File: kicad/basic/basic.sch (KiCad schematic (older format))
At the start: 20 parts, among them P2 CONN_01X15, P3 CONN_01X15, P4 CONN_01X06, P5 CONN_01X01, P6 CONN_01X01, P7 CONN_01X01, P8 CONN_01X01, P9 CONN_01X06, SW1 SW_PUSH, SW2 SW_PUSH

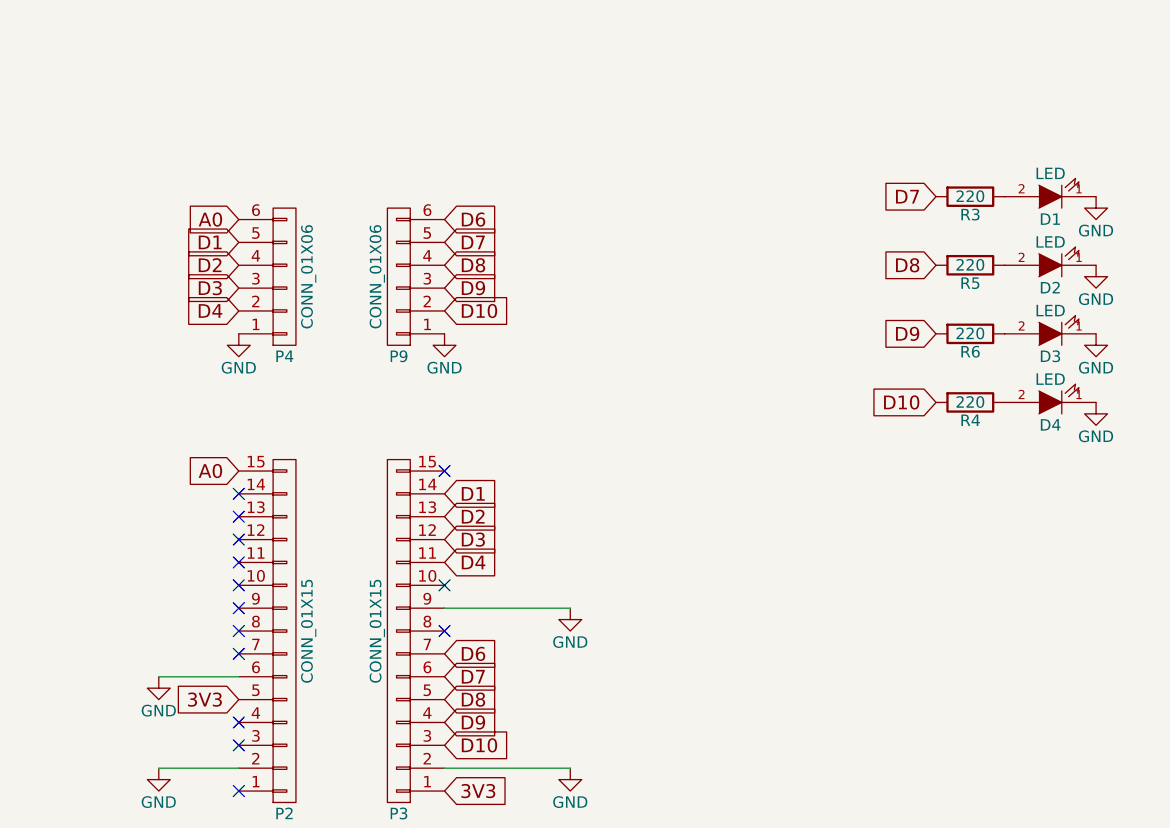
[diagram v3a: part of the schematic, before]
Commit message: RGB led
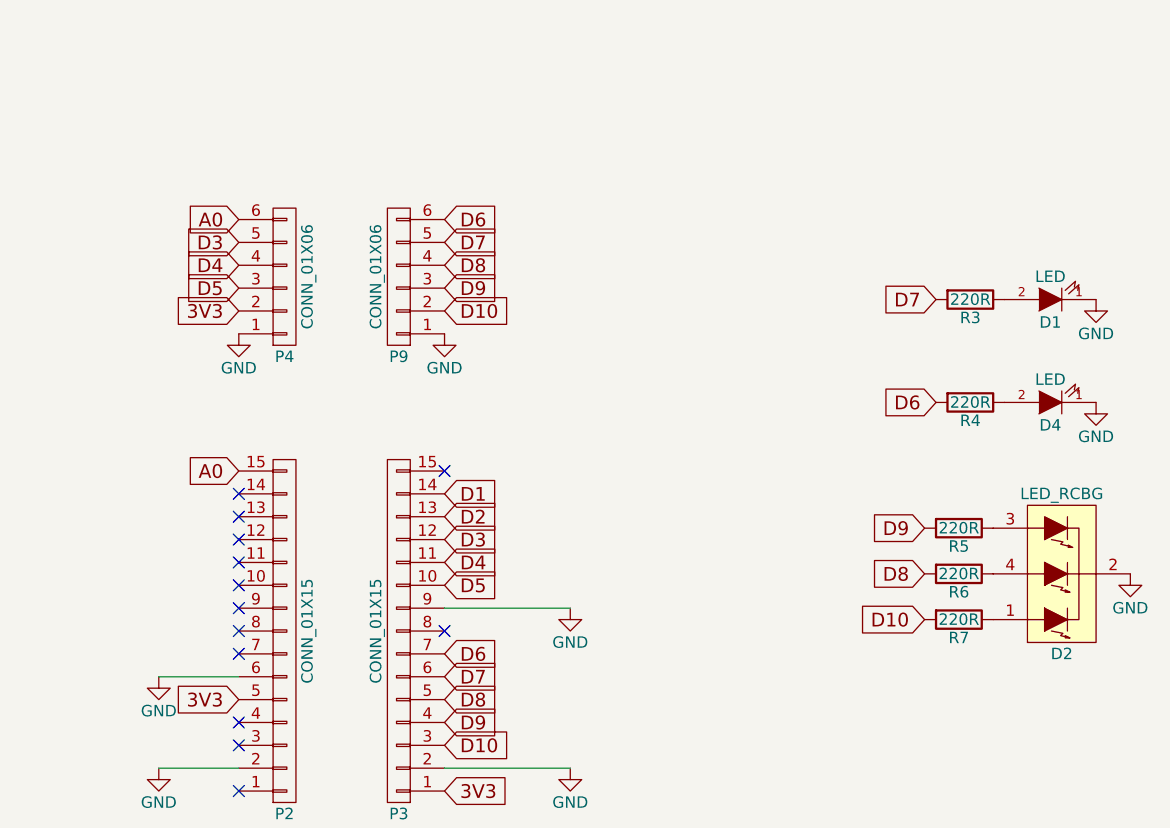
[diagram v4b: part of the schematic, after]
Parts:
- removed D2, D3: LED, LEDs:LED-5MM, symbol LED
- added D2: LED_RCBG, LEDs:LED-RGB-5MM_Common_Cathode, symbol LED_RCBG
- added R7: 220R, Resistors_ThroughHole:Resistor_Horizontal_RM10mm, symbol R
- R3, R4, R5, R6: value 220 -> 220R
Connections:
- net 3V3: now also P4.2 (P2)
- net D1: no longer P4.5 (P5)
- net D10: now also R7.2; no longer R4.2
- net D2: no longer P4.4 (P4)
- net D3: now also P4.5 (P5); no longer P4.3 (P3)
- net D4: now also P4.4 (P4); no longer P4.2 (P2)
- net D6: now also R4.2
- net D8: now also R6.2; no longer R5.2
- net D9: now also R5.2; no longer R6.2
- net GND: now also D2.2 (COMMON_CATHODE)
- net at R6.1: now also D2.4 (GREEN_ANODE)
- net at R5.1: now also D2.3 (BLUE_ANODE)
- net D5: now reaches P3.10 (P10)
- net D5: now also P4.3 (P3)
- new net: D2.1 (RED_ANODE), R7.1
- no-connect marks 14 -> 13
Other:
- moved on the sheet: D1, R3, R5, R6
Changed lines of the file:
@@
 P 8700 3200
 F 0 "R4" V 8780 3200 50  0000 C CNN
-F 1 "220" V 8700 3200 50  0000 C CNN
+F 1 "220R" V 8700 3200 50  0000 C CNN
 F 2 "Resistors_ThroughHole:Resistor_Horizontal_RM10mm" V 8630 3200 50  0001 C CNN
 F 3 "" H 8700 3200 50  0000 C CNN
@@
 $EndComp
 $Comp
-L LED D3
-U 1 1 570F8E13
-P 9050 2900
-F 0 "D3" H 9050 3000 50  0000 C CNN
-F 1 "LED" H 9050 2800 50  0000 C CNN
-F 2 "LEDs:LED-5MM" H 9050 2900 50  0001 C CNN
-F 3 "" H 9050 2900 50  0000 C CNN
-	1    9050 2900
-	-1   0    0    1
-$EndComp
-$Comp
 L R R6
 U 1 1 570F8E19
-P 8700 2900
-F 0 "R6" V 8780 2900 50  0000 C CNN
-F 1 "220" V 8700 2900 50  0000 C CNN
-F 2 "Resistors_ThroughHole:Resistor_Horizontal_RM10mm" V 8630 2900 50  0001 C CNN
-F 3 "" H 8700 2900 50  0000 C CNN
-	1    8700 2900
+P 8650 3950
+F 0 "R6" V 8730 3950 50  0000 C CNN
+F 1 "220R" V 8650 3950 50  0000 C CNN
+F 2 "Resistors_ThroughHole:Resistor_Horizontal_RM10mm" V 8580 3950 50  0001 C CNN
+F 3 "" H 8650 3950 50  0000 C CNN
+	1    8650 3950
 	0    1    1    0
-$EndComp
-$Comp
-L LED D2
-U 1 1 570F8EB1
-P 9050 2600
-F 0 "D2" H 9050 2700 50  0000 C CNN
-F 1 "LED" H 9050 2500 50  0000 C CNN
-F 2 "LEDs:LED-5MM" H 9050 2600 50  0001 C CNN
-F 3 "" H 9050 2600 50  0000 C CNN
-	1    9050 2600
-	-1   0    0    1
 $EndComp
 $Comp
 L R R5
 U 1 1 570F8EB7
-P 8700 2600
-F 0 "R5" V 8780 2600 50  0000 C CNN
-F 1 "220" V 8700 2600 50  0000 C CNN
-F 2 "Resistors_ThroughHole:Resistor_Horizontal_RM10mm" V 8630 2600 50  0001 C CNN
-F 3 "" H 8700 2600 50  0000 C CNN
-	1    8700 2600
+P 8650 3750
+F 0 "R5" V 8730 3750 50  0000 C CNN
+F 1 "220R" V 8650 3750 50  0000 C CNN
+F 2 "Resistors_ThroughHole:Resistor_Horizontal_RM10mm" V 8580 3750 50  0001 C CNN
+F 3 "" H 8650 3750 50  0000 C CNN
+	1    8650 3750
 	0    1    1    0
 $EndComp
@@
 L LED D1
 U 1 1 570F8EBD
-P 9050 2300
-F 0 "D1" H 9050 2400 50  0000 C CNN
-F 1 "LED" H 9050 2200 50  0000 C CNN
-F 2 "LEDs:LED-5MM" H 9050 2300 50  0001 C CNN
-F 3 "" H 9050 2300 50  0000 C CNN
-	1    9050 2300
+P 9050 2750
+F 0 "D1" H 9050 2850 50  0000 C CNN
+F 1 "LED" H 9050 2650 50  0000 C CNN
+F 2 "LEDs:LED-5MM" H 9050 2750 50  0001 C CNN
+F 3 "" H 9050 2750 50  0000 C CNN
+	1    9050 2750
 	-1   0    0    1
 $EndComp
@@
 L R R3
 U 1 1 570F8EC3
-P 8700 2300
-F 0 "R3" V 8780 2300 50  0000 C CNN
-F 1 "220" V 8700 2300 50  0000 C CNN
-F 2 "Resistors_ThroughHole:Resistor_Horizontal_RM10mm" V 8630 2300 50  0001 C CNN
-F 3 "" H 8700 2300 50  0000 C CNN
-	1    8700 2300
+P 8700 2750
+F 0 "R3" V 8780 2750 50  0000 C CNN
+F 1 "220R" V 8700 2750 50  0000 C CNN
+F 2 "Resistors_ThroughHole:Resistor_Horizontal_RM10mm" V 8630 2750 50  0001 C CNN
+F 3 "" H 8700 2750 50  0000 C CNN
+	1    8700 2750
 	0    1    1    0
 $EndComp
 $Comp
 L GND #PWR06
-U 1 1 570F8F9B
-P 9250 2900
-F 0 "#PWR06" H 9250 2650 50  0001 C CNN
-F 1 "GND" H 9250 2750 50  0000 C CNN
-F 2 "" H 9250 2900 50  0000 C CNN
-F 3 "" H 9250 2900 50  0000 C CNN
-	1    9250 2900
+U 1 1 570F8FDF
+P 9400 3950
+F 0 "#PWR06" H 9400 3700 50  0001 C CNN
+F 1 "GND" H 9400 3800 50  0000 C CNN
+F 2 "" H 9400 3950 50  0000 C CNN
+F 3 "" H 9400 3950 50  0000 C CNN
+	1    9400 3950
 	1    0    0    -1
 $EndComp
 $Comp
 L GND #PWR07
-U 1 1 570F8FDF
-P 9250 2600
-F 0 "#PWR07" H 9250 2350 50  0001 C CNN
-F 1 "GND" H 9250 2450 50  0000 C CNN
-F 2 "" H 9250 2600 50  0000 C CNN
-F 3 "" H 9250 2600 50  0000 C CNN
-	1    9250 2600
-	1    0    0    -1
-$EndComp
-$Comp
-L GND #PWR08
 U 1 1 570F9023
-P 9250 2300
-F 0 "#PWR08" H 9250 2050 50  0001 C CNN
-F 1 "GND" H 9250 2150 50  0000 C CNN
-F 2 "" H 9250 2300 50  0000 C CNN
-F 3 "" H 9250 2300 50  0000 C CNN
-	1    9250 2300
+P 9250 2750
+F 0 "#PWR07" H 9250 2500 50  0001 C CNN
+F 1 "GND" H 9250 2600 50  0000 C CNN
+F 2 "" H 9250 2750 50  0000 C CNN
+F 3 "" H 9250 2750 50  0000 C CNN
+	1    9250 2750
 	1    0    0    -1
 $EndComp
@@
 $EndComp
 $Comp
-L GND #PWR09
+L GND #PWR08
 U 1 1 570F9FDE
 P 6950 4800
-F 0 "#PWR09" H 6950 4550 50  0001 C CNN
+F 0 "#PWR08" H 6950 4550 50  0001 C CNN
 F 1 "GND" H 6950 4650 50  0000 C CNN
 F 2 "" H 6950 4800 50  0000 C CNN
@@
 3V3
 $Comp
-L GND #PWR010
+L GND #PWR09
 U 1 1 570FA0BF
 P 6950 4100
-F 0 "#PWR010" H 6950 3850 50  0001 C CNN
+F 0 "#PWR09" H 6950 3850 50  0001 C CNN
 F 1 "GND" H 6950 3950 50  0000 C CNN
 F 2 "" H 6950 4100 50  0000 C CNN
@@
 $EndComp
 $Comp
-L GND #PWR011
+L GND #PWR010
 U 1 1 570FA103
 P 5150 4800
-F 0 "#PWR011" H 5150 4550 50  0001 C CNN
+F 0 "#PWR010" H 5150 4550 50  0001 C CNN
 F 1 "GND" H 5150 4650 50  0000 C CNN
 F 2 "" H 5150 4800 50  0000 C CNN
@@
 $EndComp
 $Comp
-L GND #PWR012
+L GND #PWR011
 U 1 1 570FA147
 P 5150 4400
-F 0 "#PWR012" H 5150 4150 50  0001 C CNN
+F 0 "#PWR011" H 5150 4150 50  0001 C CNN
 F 1 "GND" H 5150 4250 50  0000 C CNN
 F 2 "" H 5150 4400 50  0000 C CNN
@@
 	3850 3050 3850 3200
 $Comp
-L GND #PWR013
+L GND #PWR012
 U 1 1 570FB498
 P 3850 2650
-F 0 "#PWR013" H 3850 2400 50  0001 C CNN
+F 0 "#PWR012" H 3850 2400 50  0001 C CNN
 F 1 "GND" H 3850 2500 50  0000 C CNN
 F 2 "" H 3850 2650 50  0000 C CNN
@@
 $EndComp
 $Comp
-L GND #PWR014
+L GND #PWR013
 U 1 1 570FB53B
 P 3850 3500
-F 0 "#PWR014" H 3850 3250 50  0001 C CNN
+F 0 "#PWR013" H 3850 3250 50  0001 C CNN
 F 1 "GND" H 3850 3350 50  0000 C CNN
 F 2 "" H 3850 3500 50  0000 C CNN
@@
 $EndComp
 $Comp
-L GND #PWR015
+L GND #PWR014
 U 1 1 570FA133
 P 6400 2900
-F 0 "#PWR015" H 6400 2650 50  0001 C CNN
+F 0 "#PWR014" H 6400 2650 50  0001 C CNN
 F 1 "GND" H 6400 2750 50  0000 C CNN
 F 2 "" H 6400 2900 50  0000 C CNN
@@
 $EndComp
 $Comp
-L GND #PWR016
+L GND #PWR015
 U 1 1 570FA17D
 P 5500 2900
-F 0 "#PWR016" H 5500 2650 50  0001 C CNN
+F 0 "#PWR015" H 5500 2650 50  0001 C CNN
 F 1 "GND" H 5500 2750 50  0000 C CNN
 F 2 "" H 5500 2900 50  0000 C CNN
@@
 D6
 Text GLabel 5500 2500 0    60   Input ~ 0
-D1
+D3
 Text GLabel 5500 2600 0    60   Input ~ 0
-D2
-Text GLabel 5500 2700 0    60   Input ~ 0
-D3
-Text GLabel 5500 2800 0    60   Input ~ 0
 D4
 NoConn ~ 6400 4200
-Text GLabel 8550 3200 0    60   Input ~ 0
+Text GLabel 8500 4150 0    60   Input ~ 0
 D10
-Text GLabel 8550 2900 0    60   Input ~ 0
+Text GLabel 8500 3750 0    60   Input ~ 0
 D9
-Text GLabel 8550 2600 0    60   Input ~ 0
+Text GLabel 8500 3950 0    60   Input ~ 0
 D8
-Text GLabel 8550 2300 0    60   Input ~ 0
+Text GLabel 8550 2750 0    60   Input ~ 0
 D7
 Text GLabel 3850 2200 2    60   Input ~ 0
@@
 Text GLabel 3850 3050 2    60   Input ~ 0
 D2
-NoConn ~ 6400 4000
+$Comp
+L LED_RCBG D2
+U 1 1 571157B6
+P 9100 3950
+F 0 "D2" H 9100 4300 50  0000 C CNN
+F 1 "LED_RCBG" H 9100 3600 50  0000 C CNN
+F 2 "LEDs:LED-RGB-5MM_Common_Cathode" H 9100 3900 50  0001 C CNN
+F 3 "" H 9100 3900 50  0000 C CNN
+	1    9100 3950
+	-1   0    0    1
+$EndComp
+Text GLabel 8550 3200 0    60   Input ~ 0
+D6
+$Comp
+L R R7
+U 1 1 57115CAD
+P 8650 4150
+F 0 "R7" V 8730 4150 50  0000 C CNN
+F 1 "220R" V 8650 4150 50  0000 C CNN
+F 2 "Resistors_ThroughHole:Resistor_Horizontal_RM10mm" V 8580 4150 50  0001 C CNN
+F 3 "" H 8650 4150 50  0000 C CNN
+	1    8650 4150
+	0    1    1    0
+$EndComp
+Text GLabel 6400 4000 2    60   Input ~ 0
+D5
+Text GLabel 5500 2700 0    60   Input ~ 0
+D5
+Text GLabel 5500 2800 0    60   Input ~ 0
+3V3
 $EndSCHEMATC

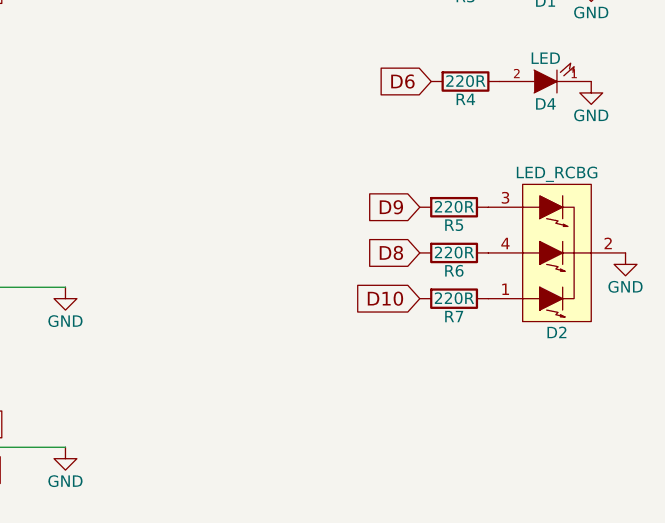
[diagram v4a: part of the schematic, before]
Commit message: Layout tweaks
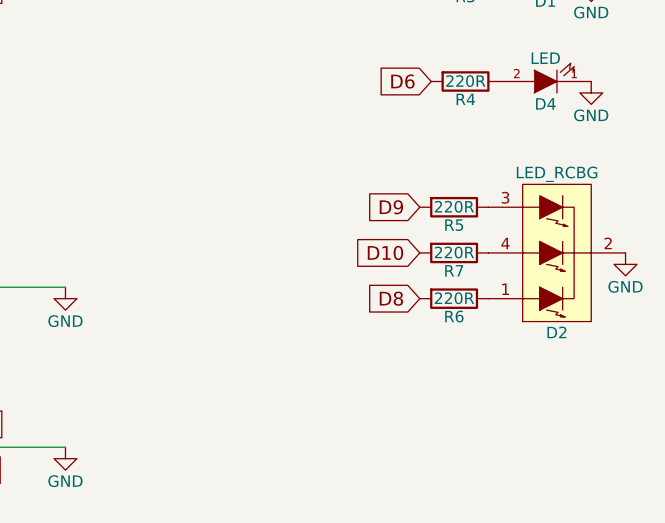
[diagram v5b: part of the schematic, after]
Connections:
- net at R6.1: now also D2.1 (RED_ANODE); no longer D2.4 (GREEN_ANODE)
- net at R7.1: now also D2.4 (GREEN_ANODE); no longer D2.1 (RED_ANODE)
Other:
- moved on the sheet: R6, R7
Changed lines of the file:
@@
 L R R6
 U 1 1 570F8E19
-P 8650 3950
-F 0 "R6" V 8730 3950 50  0000 C CNN
-F 1 "220R" V 8650 3950 50  0000 C CNN
-F 2 "Resistors_ThroughHole:Resistor_Horizontal_RM10mm" V 8580 3950 50  0001 C CNN
-F 3 "" H 8650 3950 50  0000 C CNN
-	1    8650 3950
+P 8650 4150
+F 0 "R6" V 8730 4150 50  0000 C CNN
+F 1 "220R" V 8650 4150 50  0000 C CNN
+F 2 "Resistors_ThroughHole:Resistor_Horizontal_RM10mm" V 8580 4150 50  0001 C CNN
+F 3 "" H 8650 4150 50  0000 C CNN
+	1    8650 4150
 	0    1    1    0
 $EndComp
@@
 D4
 NoConn ~ 6400 4200
-Text GLabel 8500 4150 0    60   Input ~ 0
+Text GLabel 8500 3950 0    60   Input ~ 0
 D10
 Text GLabel 8500 3750 0    60   Input ~ 0
 D9
-Text GLabel 8500 3950 0    60   Input ~ 0
+Text GLabel 8500 4150 0    60   Input ~ 0
 D8
 Text GLabel 8550 2750 0    60   Input ~ 0
@@
 L R R7
 U 1 1 57115CAD
-P 8650 4150
-F 0 "R7" V 8730 4150 50  0000 C CNN
-F 1 "220R" V 8650 4150 50  0000 C CNN
-F 2 "Resistors_ThroughHole:Resistor_Horizontal_RM10mm" V 8580 4150 50  0001 C CNN
-F 3 "" H 8650 4150 50  0000 C CNN
-	1    8650 4150
+P 8650 3950
+F 0 "R7" V 8730 3950 50  0000 C CNN
+F 1 "220R" V 8650 3950 50  0000 C CNN
+F 2 "Resistors_ThroughHole:Resistor_Horizontal_RM10mm" V 8580 3950 50  0001 C CNN
+F 3 "" H 8650 3950 50  0000 C CNN
+	1    8650 3950
 	0    1    1    0
 $EndComp

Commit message: Resistor values
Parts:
- R3, R4, R6: value 220R -> 150R
- R5, R7: value 220R -> 100R
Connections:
- net S_RED: now reaches D4.2 (A), R4.1
- net RGB_RED: now reaches D2.1 (RED_ANODE), R6.1
- net RGB_GREEN: now reaches D2.3 (BLUE_ANODE), R5.1
- net S_GREEN: now reaches D1.2 (A), R3.1
- net RGB_BLUE: now reaches D2.4 (GREEN_ANODE), R7.1
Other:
- moved on the sheet: R3, R4, R5, R6, R7
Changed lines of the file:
@@
 L R R4
 U 1 1 570F67D8
-P 8700 3200
-F 0 "R4" V 8780 3200 50  0000 C CNN
-F 1 "220R" V 8700 3200 50  0000 C CNN
-F 2 "Resistors_ThroughHole:Resistor_Horizontal_RM10mm" V 8630 3200 50  0001 C CNN
-F 3 "" H 8700 3200 50  0000 C CNN
-	1    8700 3200
+P 8300 3200
+F 0 "R4" V 8380 3200 50  0000 C CNN
+F 1 "150R" V 8300 3200 50  0000 C CNN
+F 2 "Resistors_ThroughHole:Resistor_Horizontal_RM10mm" V 8230 3200 50  0001 C CNN
+F 3 "" H 8300 3200 50  0000 C CNN
+	1    8300 3200
 	0    1    1    0
 $EndComp
@@
 L R R6
 U 1 1 570F8E19
-P 8650 4150
-F 0 "R6" V 8730 4150 50  0000 C CNN
-F 1 "220R" V 8650 4150 50  0000 C CNN
-F 2 "Resistors_ThroughHole:Resistor_Horizontal_RM10mm" V 8580 4150 50  0001 C CNN
-F 3 "" H 8650 4150 50  0000 C CNN
-	1    8650 4150
+P 8200 4150
+F 0 "R6" V 8280 4150 50  0000 C CNN
+F 1 "150R" V 8200 4150 50  0000 C CNN
+F 2 "Resistors_ThroughHole:Resistor_Horizontal_RM10mm" V 8130 4150 50  0001 C CNN
+F 3 "" H 8200 4150 50  0000 C CNN
+	1    8200 4150
 	0    1    1    0
 $EndComp
@@
 L R R5
 U 1 1 570F8EB7
-P 8650 3750
-F 0 "R5" V 8730 3750 50  0000 C CNN
-F 1 "220R" V 8650 3750 50  0000 C CNN
-F 2 "Resistors_ThroughHole:Resistor_Horizontal_RM10mm" V 8580 3750 50  0001 C CNN
-F 3 "" H 8650 3750 50  0000 C CNN
-	1    8650 3750
+P 8200 3750
+F 0 "R5" V 8280 3750 50  0000 C CNN
+F 1 "100R" V 8200 3750 50  0000 C CNN
+F 2 "Resistors_ThroughHole:Resistor_Horizontal_RM10mm" V 8130 3750 50  0001 C CNN
+F 3 "" H 8200 3750 50  0000 C CNN
+	1    8200 3750
 	0    1    1    0
 $EndComp
@@
 L R R3
 U 1 1 570F8EC3
-P 8700 2750
-F 0 "R3" V 8780 2750 50  0000 C CNN
-F 1 "220R" V 8700 2750 50  0000 C CNN
-F 2 "Resistors_ThroughHole:Resistor_Horizontal_RM10mm" V 8630 2750 50  0001 C CNN
-F 3 "" H 8700 2750 50  0000 C CNN
-	1    8700 2750
+P 8300 2750
+F 0 "R3" V 8380 2750 50  0000 C CNN
+F 1 "150R" V 8300 2750 50  0000 C CNN
+F 2 "Resistors_ThroughHole:Resistor_Horizontal_RM10mm" V 8230 2750 50  0001 C CNN
+F 3 "" H 8300 2750 50  0000 C CNN
+	1    8300 2750
 	0    1    1    0
 $EndComp
@@
 D4
 NoConn ~ 6400 4200
-Text GLabel 8500 3950 0    60   Input ~ 0
+Text GLabel 8050 3950 0    60   Input ~ 0
 D10
-Text GLabel 8500 3750 0    60   Input ~ 0
+Text GLabel 8050 3750 0    60   Input ~ 0
 D9
-Text GLabel 8500 4150 0    60   Input ~ 0
+Text GLabel 8050 4150 0    60   Input ~ 0
 D8
-Text GLabel 8550 2750 0    60   Input ~ 0
+Text GLabel 8150 2750 0    60   Input ~ 0
 D7
 Text GLabel 3850 2200 2    60   Input ~ 0
@@
 	-1   0    0    1
 $EndComp
-Text GLabel 8550 3200 0    60   Input ~ 0
+Text GLabel 8150 3200 0    60   Input ~ 0
 D6
 $Comp
 L R R7
 U 1 1 57115CAD
-P 8650 3950
-F 0 "R7" V 8730 3950 50  0000 C CNN
-F 1 "220R" V 8650 3950 50  0000 C CNN
-F 2 "Resistors_ThroughHole:Resistor_Horizontal_RM10mm" V 8580 3950 50  0001 C CNN
-F 3 "" H 8650 3950 50  0000 C CNN
-	1    8650 3950
+P 8200 3950
+F 0 "R7" V 8280 3950 50  0000 C CNN
+F 1 "100R" V 8200 3950 50  0000 C CNN
+F 2 "Resistors_ThroughHole:Resistor_Horizontal_RM10mm" V 8130 3950 50  0001 C CNN
+F 3 "" H 8200 3950 50  0000 C CNN
+	1    8200 3950
 	0    1    1    0
 $EndComp
@@
 Text GLabel 5500 2800 0    60   Input ~ 0
 3V3
+Wire Wire Line
+	8350 3750 8800 3750
+Wire Wire Line
+	8350 3950 8800 3950
+Wire Wire Line
+	8350 4150 8800 4150
+Text Label 8400 4150 0    60   ~ 0
+RGB_RED
+Text Label 8400 3750 0    60   ~ 0
+RGB_GREEN
+Text Label 8400 3950 0    60   ~ 0
+RGB_BLUE
+Wire Wire Line
+	8450 2750 8850 2750
+Wire Wire Line
+	8450 3200 8850 3200
+Text Label 8500 2750 0    60   ~ 0
+S_GREEN
+Text Label 8500 3200 0    60   ~ 0
+S_RED
 $EndSCHEMATC
